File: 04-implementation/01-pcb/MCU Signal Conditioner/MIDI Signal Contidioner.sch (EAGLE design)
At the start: 38 parts, among them J2 ARDUINO-CONN-8X2, J3 ARDUINO-CONN-8X2, U3 74LVC4245A, U4 24CS01, U5 PI6ULS5V9515A, U6 MCP1700-SOT89, X1 SSW-107-02-S-D, X2 SSW-107-02-S-D, X3 SSW-107-02-S-D, X4 SSW-107-02-S-D, X5 MINI-USB-SHIELD-32005-201

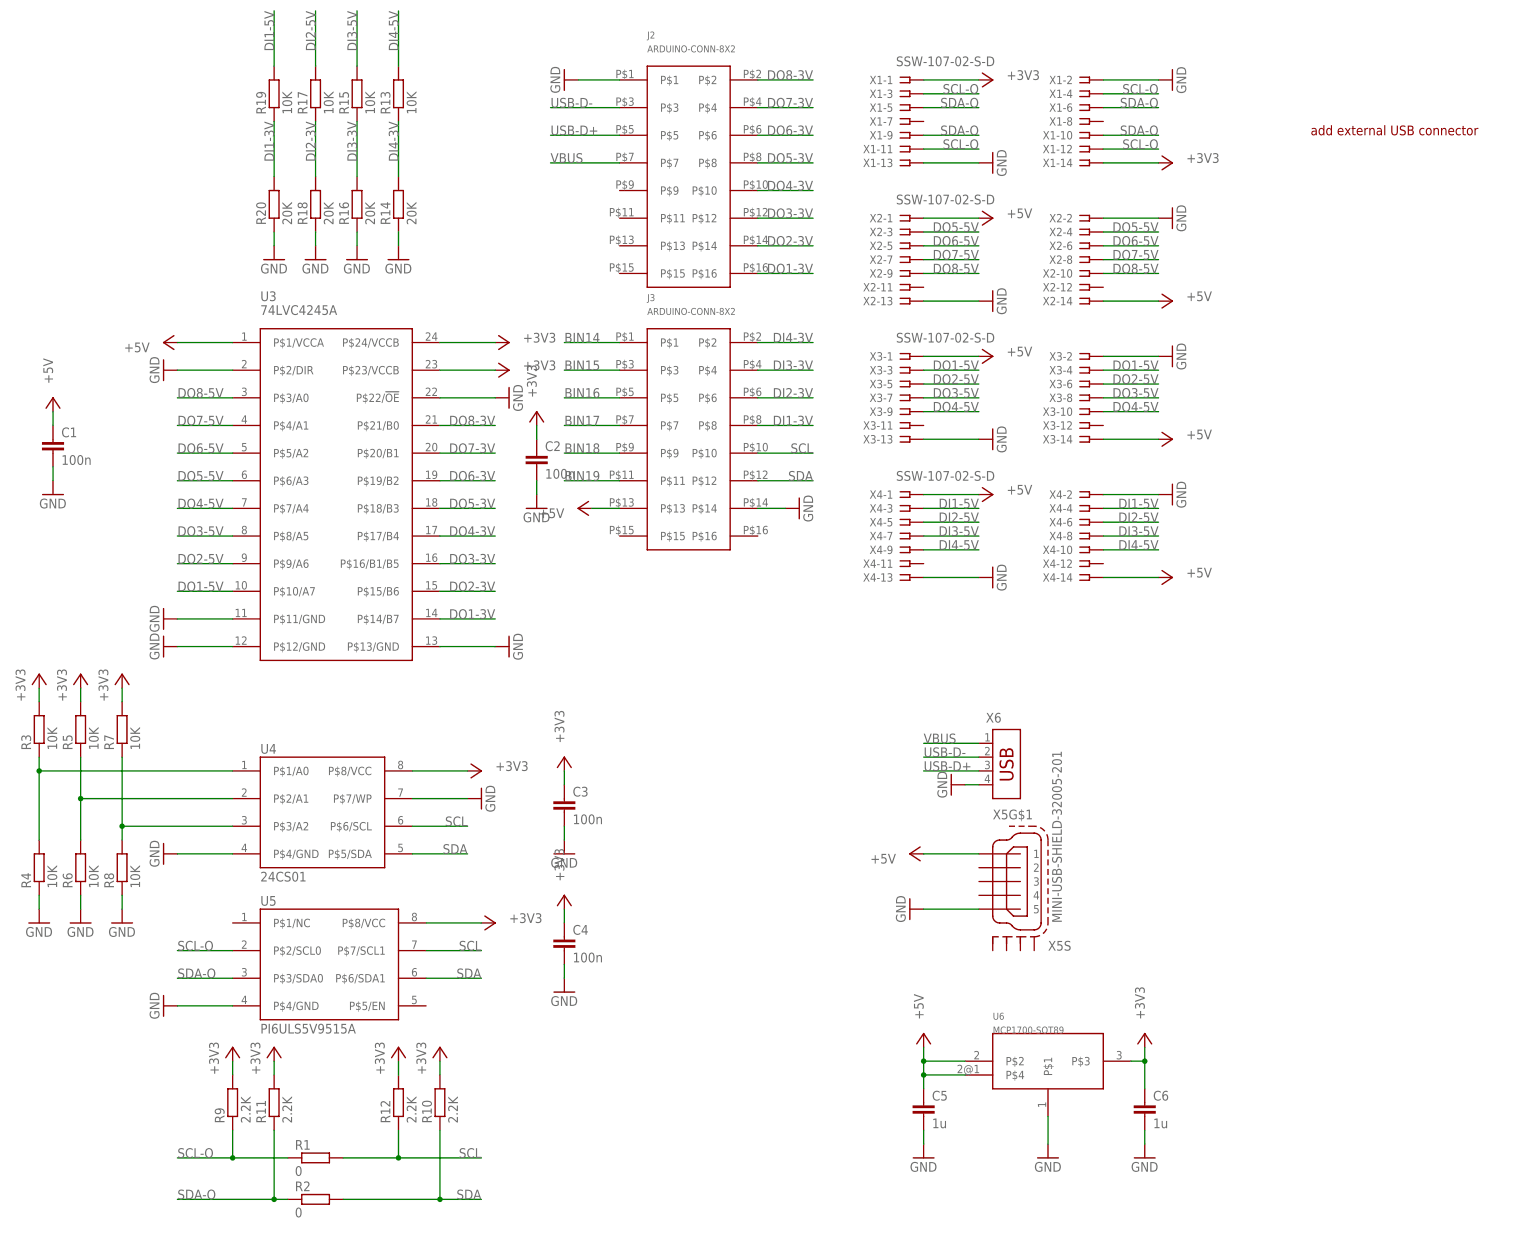
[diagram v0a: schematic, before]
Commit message: Change signal conditioner board to 3.3V rail.
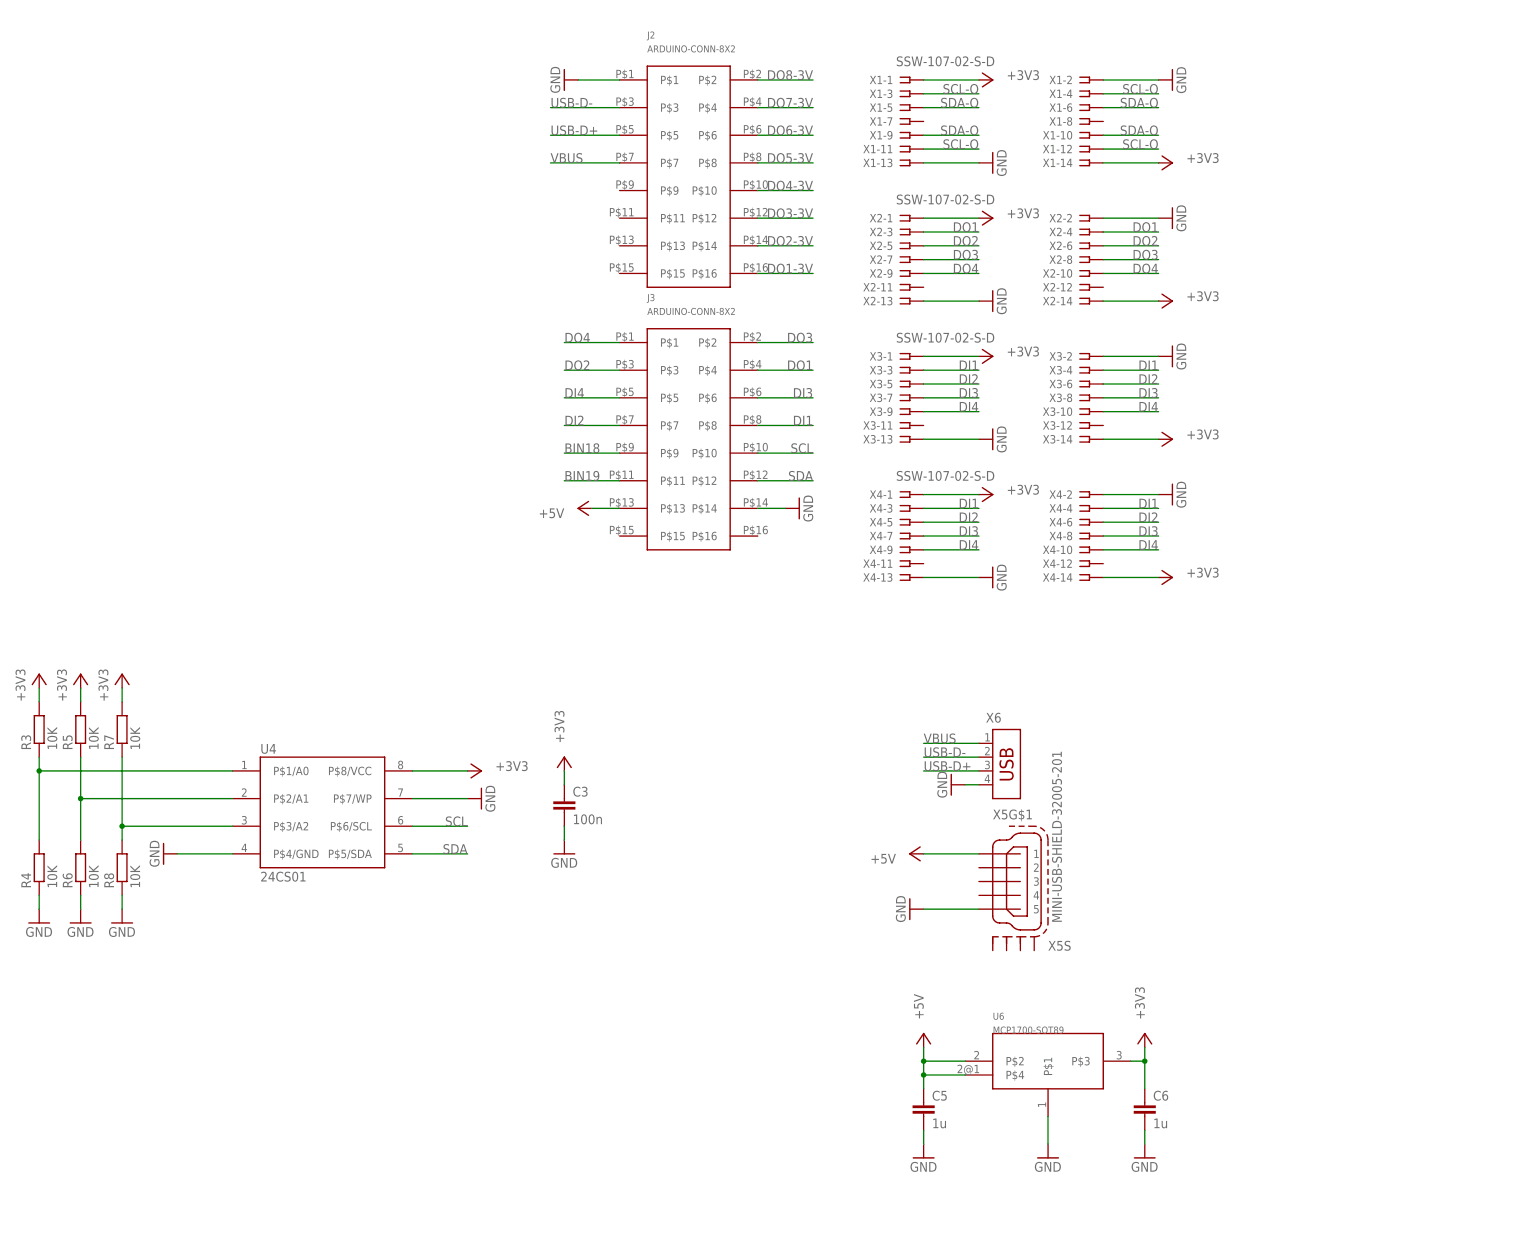
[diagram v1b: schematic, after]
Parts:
- removed C1, C2, C4: 100n, rcl:C-EUC0805
- removed R1, R2: 0, rcl:R-EU_R0805
- removed R10, R11, R12, R9: 2.2K, rcl:R-EU_R0805
- removed R13, R15, R17, R19: 10K, rcl:R-EU_R0805
- removed R14, R16, R18, R20: 20K, rcl:R-EU_R0805
- removed U3: 74LVC4245A, MIDI Signal Conditioner Parts:74LVC4245A
- removed U5: PI6ULS5V9515A, MIDI Signal Conditioner Parts:PI6ULS5V9515A
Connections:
- removed net BIN14: J3.P$1
- removed net BIN15: J3.P$3
- removed net BIN16: J3.P$5
- removed net BIN17: J3.P$7
- removed net DI1-3V: J3.P$8, R19.1, R20.2
- removed net DI1-5V: R19.2, X4-3.1, X4-4.1
- removed net DI2-3V: J3.P$6, R17.1, R18.2
- removed net DI2-5V: R17.2, X4-5.1, X4-6.1
- removed net DI3-3V: J3.P$4, R15.1, R16.2
- removed net DI3-5V: R15.2, X4-7.1, X4-8.1
- removed net DI4-3V: J3.P$2, R13.1, R14.2
- removed net DI4-5V: R13.2, X4-10.1, X4-9.1
- removed net DO1-5V: U3.P$10/A7, X3-3.1, X3-4.1
- removed net DO2-5V: U3.P$9/A6, X3-5.1, X3-6.1
- removed net DO3-5V: U3.P$8/A5, X3-7.1, X3-8.1
- removed net DO4-5V: U3.P$7/A4, X3-10.1, X3-9.1
- removed net DO5-5V: U3.P$6/A3, X2-3.1, X2-4.1
- removed net DO6-5V: U3.P$5/A2, X2-5.1, X2-6.1
- removed net DO7-5V: U3.P$4/A1, X2-7.1, X2-8.1
- removed net DO8-5V: U3.P$3/A0, X2-10.1, X2-9.1
- new net DI1: J3.P$8, X3-3.1, X3-4.1, X4-3.1, X4-4.1
- new net DI2: J3.P$7, X3-5.1, X3-6.1, X4-5.1, X4-6.1
- new net DI3: J3.P$6, X3-7.1, X3-8.1, X4-7.1, X4-8.1
- new net DI4: J3.P$5, X3-10.1, X3-9.1, X4-10.1, X4-9.1
- new net DO1: J3.P$4, X2-3.1, X2-4.1
- new net DO2: J3.P$3, X2-5.1, X2-6.1
- new net DO3: J3.P$2, X2-7.1, X2-8.1
- new net DO4: J3.P$1, X2-10.1, X2-9.1
- net +3V3: now also X2-1.1, X2-14.1, X3-1.1, X3-14.1, X4-1.1, X4-14.1; no longer C2.1, C4.1, R10.2, R11.2, R12.2, R9.2, U3.P$23/VCCB, U3.P$24/VCCB, U5.P$8/VCC
- net +5V: no longer C1.1, U3.P$1/VCCA, X2-1.1, X2-14.1, X3-1.1, X3-14.1, X4-1.1, X4-14.1
- net DO1-3V: no longer U3.P$14/B7
- net DO2-3V: no longer U3.P$15/B6
- net DO3-3V: no longer U3.P$16/B1/B5
- net DO4-3V: no longer U3.P$17/B4
- net DO5-3V: no longer U3.P$18/B3
- net DO6-3V: no longer U3.P$19/B2
- net DO7-3V: no longer U3.P$20/B1
- net DO8-3V: no longer U3.P$21/B0
- net GND: no longer C1.2, C2.2, C4.2, R14.1, R16.1, R18.1, R20.1, U3.P$11/GND, U3.P$12/GND, U3.P$13/GND, U3.P$2/DIR, U3.P$22/!OE, U5.P$4/GND
- net SCL: no longer R1.2, R12.1, U5.P$7/SCL1
- net SCL-O: no longer R1.1, R9.1, U5.P$2/SCL0
- net SDA: no longer R10.1, R2.2, U5.P$6/SDA1
- net SDA-O: no longer R11.1, R2.1, U5.P$3/SDA0
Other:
- note removed: "add external USB connector"

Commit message: Update signal conditioner.
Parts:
- removed R3, R4, R5, R6, R7, R8: 10K, rcl:R-EU_R0805
- added R1, R2: 2.2K, rcl:R-EU_R0805W
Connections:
- removed net DO1-3V: J2.P$16
- removed net DO2-3V: J2.P$14
- removed net DO3-3V: J2.P$12
- removed net DO4-3V: J2.P$10
- removed net DO5-3V: J2.P$8
- removed net DO6-3V: J2.P$6
- removed net DO7-3V: J2.P$4
- removed net DO8-3V: J2.P$2
- removed net N$1: R3.1, R4.2, U4.P$1/A0
- removed net N$2: R5.1, R6.2, U4.P$2/A1
- removed net N$3: R7.1, R8.2, U4.P$3/A2
- removed net SCL-O: X1-11.1, X1-12.1, X1-3.1, X1-4.1
- removed net SDA-O: X1-10.1, X1-5.1, X1-6.1, X1-9.1
- net +3V3: now also R1.1, R2.1; no longer R3.2, R5.2, R7.2
- net GND: now also U4.P$1/A0, U4.P$2/A1, U4.P$3/A2; no longer R4.1, R6.1, R8.1
- net SCL: now also R1.2, X1-11.1, X1-12.1
- net SDA: now also R2.2, X1-10.1, X1-9.1
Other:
- moved on the sheet: C3, C5, C6, J2, J3, U4, U6, X1-1, X1-10, X1-11, X1-12, X1-13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

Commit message: Complete initial placement of components.
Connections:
- net GND: now also X5S.S1, X5S.S2, X5S.S3, X5S.S4
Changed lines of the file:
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@@
 <part name="+3V1" library="supply1" library_urn="urn:adsk.eagle:library:371" deviceset="+3V3" device=""/>
 <part name="+3V2" library="supply1" library_urn="urn:adsk.eagle:library:371" deviceset="+3V3" device=""/>
+<part name="GND10" library="supply1" library_urn="urn:adsk.eagle:library:371" deviceset="GND" device=""/>
+<part name="GND11" library="supply1" library_urn="urn:adsk.eagle:library:371" deviceset="GND" device=""/>
 </parts>
 <sheets>
@@
 <attribute name="VALUE" x="215.9" y="2.54" size="1.778" layer="96" rot="R90"/>
 </instance>
+<instance part="GND10" gate="1" x="228.6" y="-111.76"/>
+<instance part="GND11" gate="1" x="236.22" y="-111.76"/>
 </instances>
 <busses>
@@
 <wire x1="154.94" y1="-35.56" x2="165.1" y2="-35.56" width="0.1524" layer="91"/>
 </segment>
+<segment>
+<pinref part="X5" gate="S" pin="S4"/>
+<pinref part="GND11" gate="1" pin="GND"/>
+<wire x1="236.22" y1="-104.14" x2="236.22" y2="-106.68" width="0.1524" layer="91"/>
+<pinref part="X5" gate="S" pin="S3"/>
+<wire x1="236.22" y1="-106.68" x2="236.22" y2="-109.22" width="0.1524" layer="91"/>
+<wire x1="233.68" y1="-104.14" x2="233.68" y2="-106.68" width="0.1524" layer="91"/>
+<wire x1="233.68" y1="-106.68" x2="236.22" y2="-106.68" width="0.1524" layer="91"/>
+<junction x="236.22" y="-106.68"/>
+</segment>
+<segment>
+<pinref part="X5" gate="S" pin="S1"/>
+<pinref part="GND10" gate="1" pin="GND"/>
+<wire x1="228.6" y1="-104.14" x2="228.6" y2="-106.68" width="0.1524" layer="91"/>
+<pinref part="X5" gate="S" pin="S2"/>
+<wire x1="228.6" y1="-106.68" x2="228.6" y2="-109.22" width="0.1524" layer="91"/>
+<wire x1="231.14" y1="-104.14" x2="231.14" y2="-106.68" width="0.1524" layer="91"/>
+<wire x1="231.14" y1="-106.68" x2="228.6" y2="-106.68" width="0.1524" layer="91"/>
+<junction x="228.6" y="-106.68"/>
+</segment>
 </net>

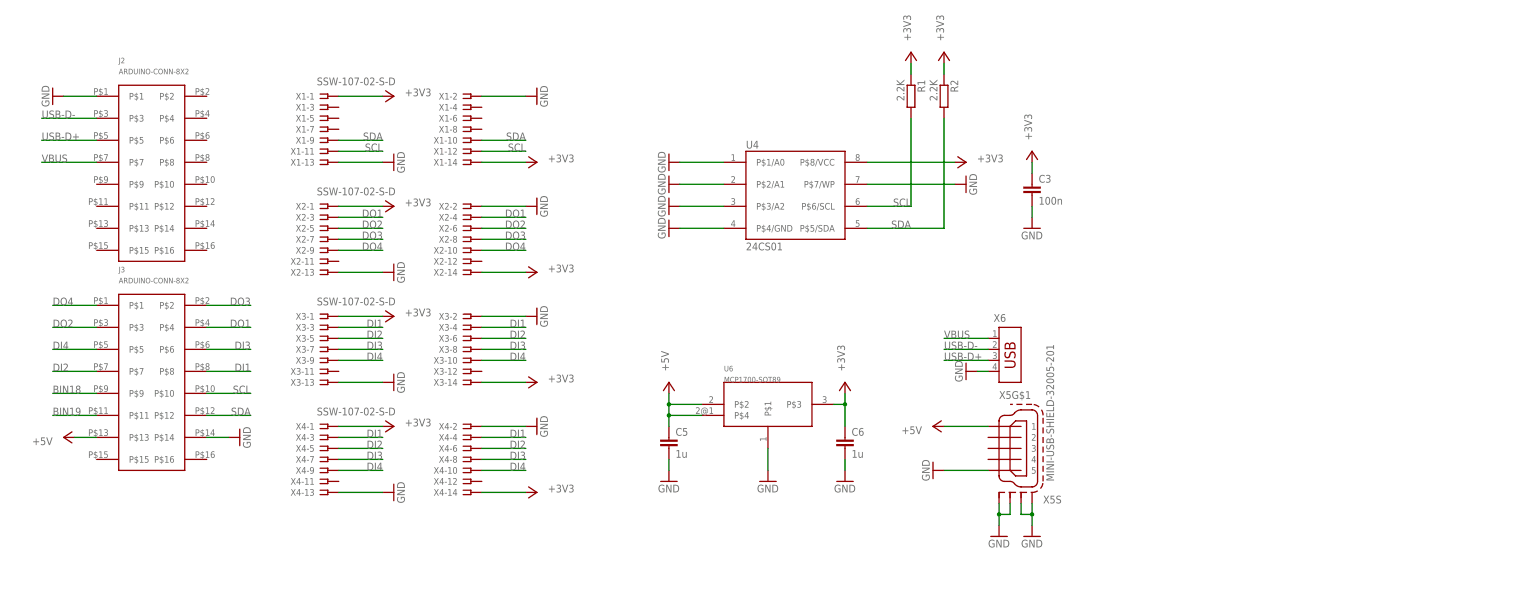
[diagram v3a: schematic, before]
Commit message: Complete initial placement of signal conditioning board (5V).
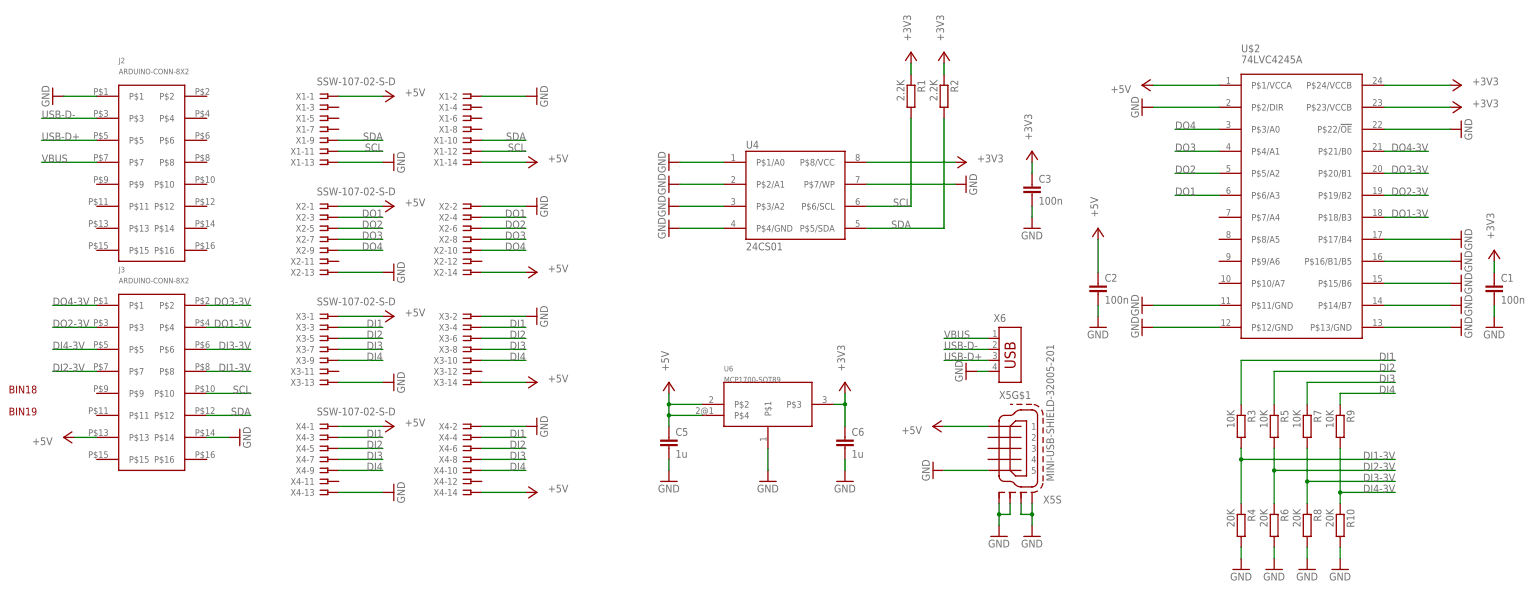
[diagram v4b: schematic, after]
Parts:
- added C1, C2: 100n, rcl:C-EUC0805
- added R10, R4, R6, R8: 20K, rcl:R-EU_R0805W
- added R3, R5, R7, R9: 10K, rcl:R-EU_R0805W
- added U$2: 74LVC4245A, MIDI Signal Conditioner Parts:74LVC4245A
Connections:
- removed net BIN18: J3.P$9
- removed net BIN19: J3.P$11
- new net DI1-3V: J3.P$8, R3.2, R4.1
- new net DI2-3V: J3.P$7, R5.2, R6.1
- new net DI3-3V: J3.P$6, R7.2, R8.1
- new net DI4-3V: J3.P$5, R10.1, R9.2
- new net DO1-3V: J3.P$4, U$2.P$18/B3
- new net DO2-3V: J3.P$3, U$2.P$19/B2
- new net DO3-3V: J3.P$2, U$2.P$20/B1
- new net DO4-3V: J3.P$1, U$2.P$21/B0
- net +3V3: now also C1.1, U$2.P$23/VCCB, U$2.P$24/VCCB; no longer X1-1.1, X1-14.1, X2-1.1, X2-14.1, X3-1.1, X3-14.1, X4-1.1, X4-14.1
- net +5V: now also C2.1, U$2.P$1/VCCA, X1-1.1, X1-14.1, X2-1.1, X2-14.1, X3-1.1, X3-14.1, X4-1.1, X4-14.1
- net DI1: now also R3.1; no longer J3.P$8
- net DI2: now also R5.1; no longer J3.P$7
- net DI3: now also R7.1; no longer J3.P$6
- net DI4: now also R9.1; no longer J3.P$5
- net DO1: now also U$2.P$6/A3; no longer J3.P$4
- net DO2: now also U$2.P$5/A2; no longer J3.P$3
- net DO3: now also U$2.P$4/A1; no longer J3.P$2
- net DO4: now also U$2.P$3/A0; no longer J3.P$1
- net GND: now also C1.2, C2.2, R10.2, R4.2, R6.2, R8.2, U$2.P$11/GND, U$2.P$12/GND, U$2.P$13/GND, U$2.P$14/B7, U$2.P$15/B6, U$2.P$16/B1/B5, U$2.P$17/B4, U$2.P$2/DIR, U$2.P$22/!OE
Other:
- note added: "BIN18"
- note added: "BIN19"
